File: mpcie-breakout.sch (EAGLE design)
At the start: 43 parts, among them K1 694108106102, U1 IP4234CZ6, U2 LD1085D2T33R, X1 MPCIE-JAE, X2 MINI-USB-SHIELD-UX60-MB-5ST

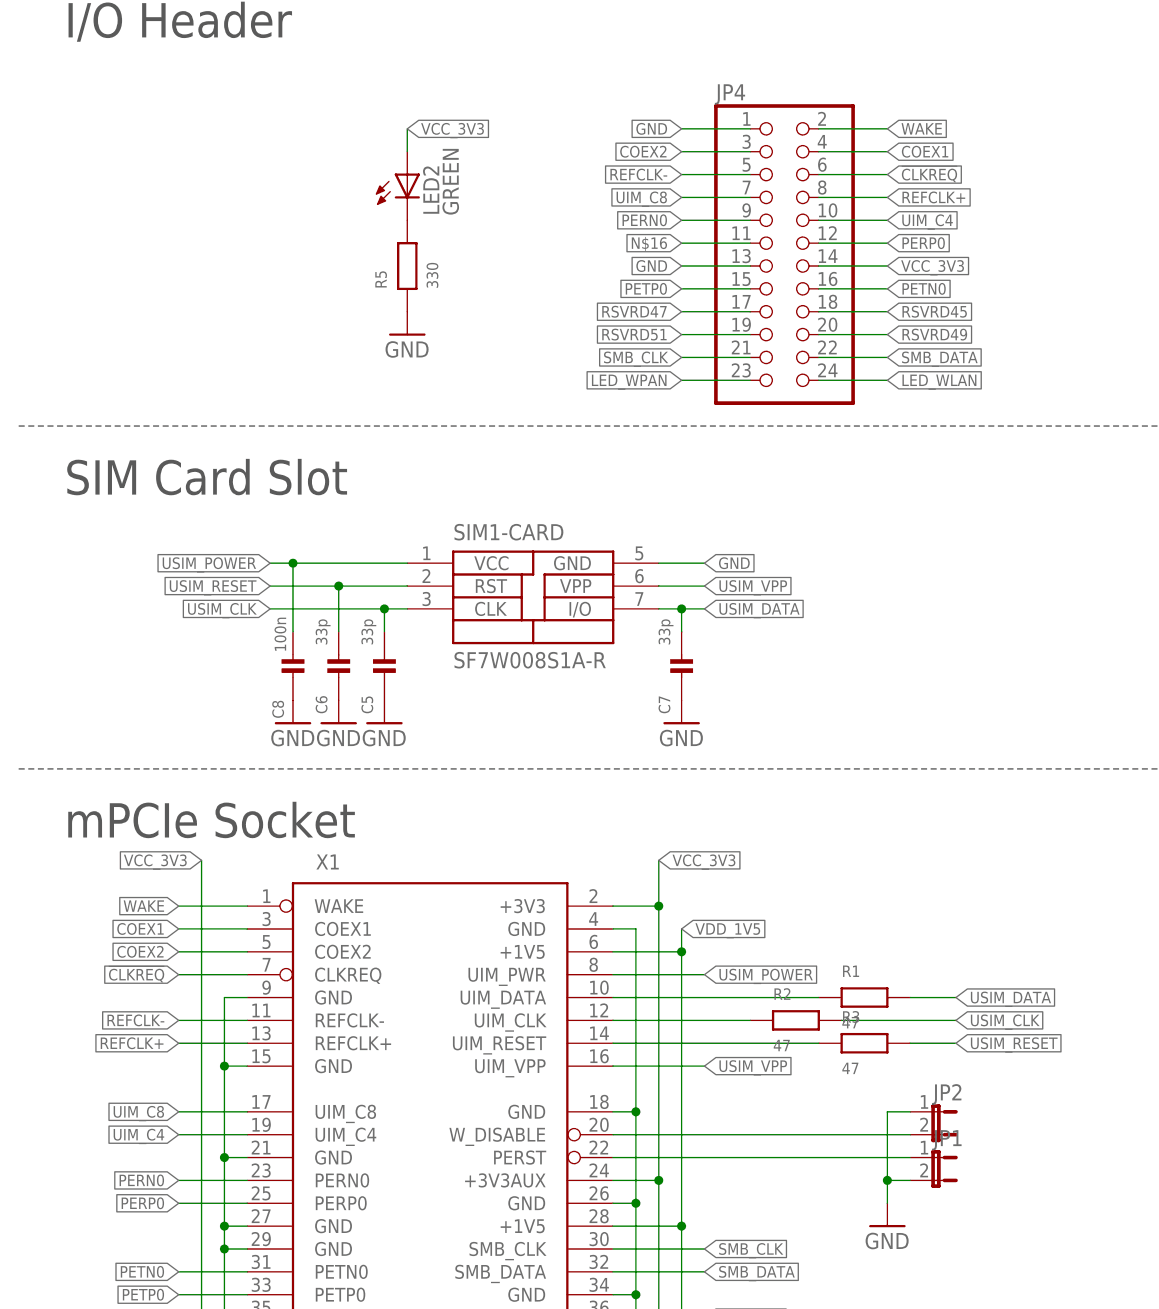
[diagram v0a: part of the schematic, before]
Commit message: added RXD, TXD, RTS, CTS
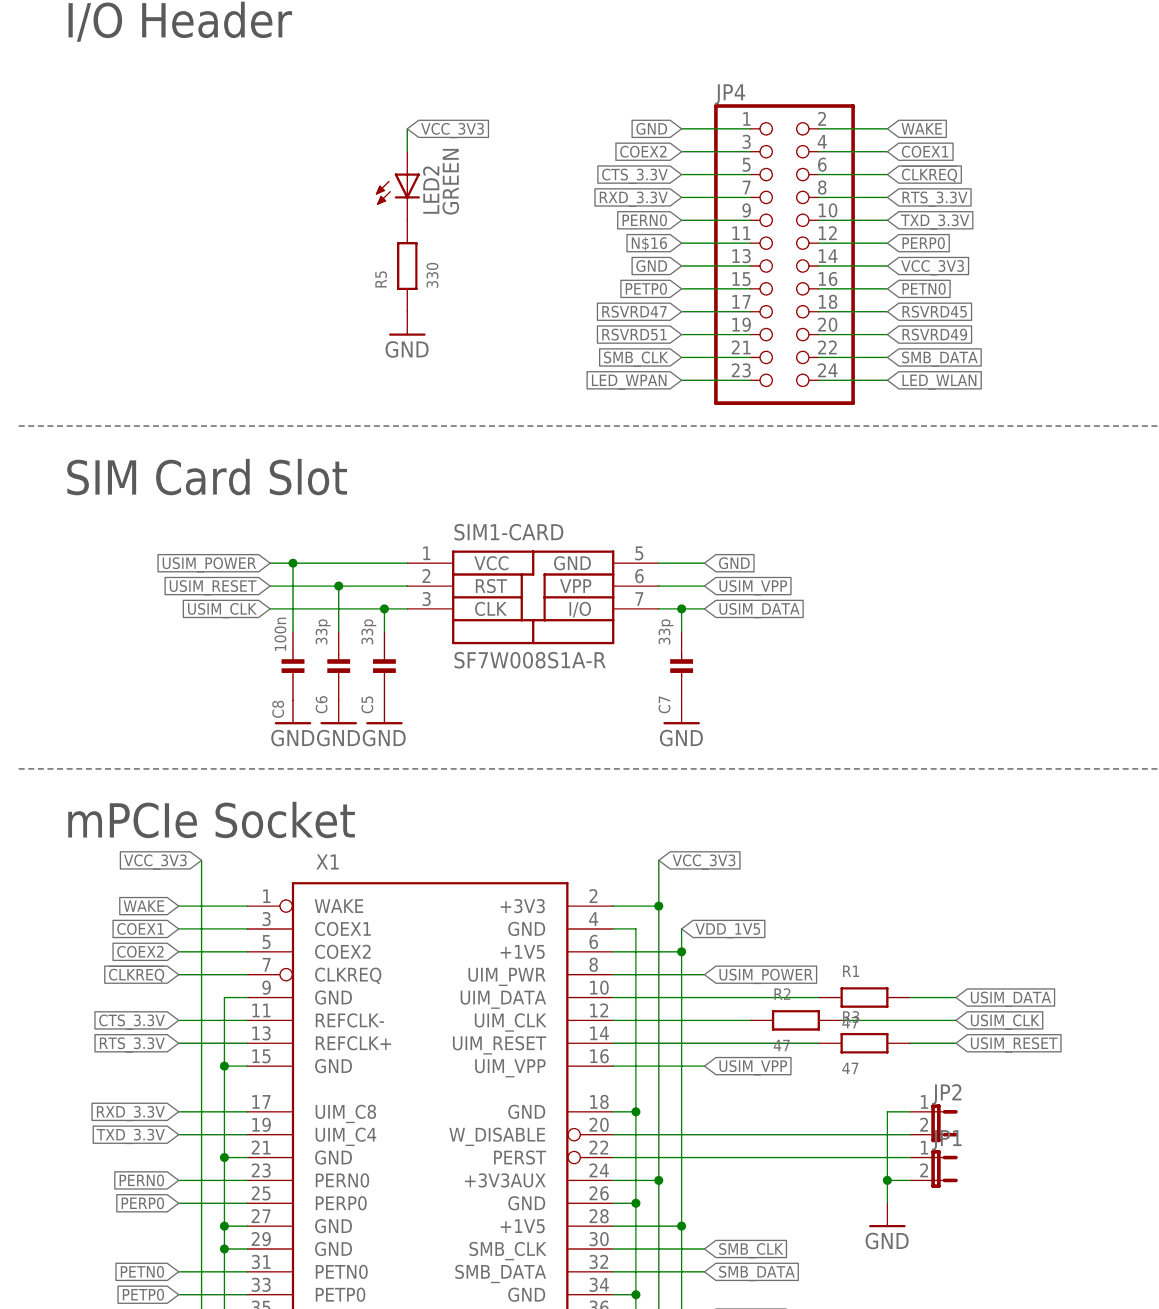
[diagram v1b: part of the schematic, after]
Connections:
- net REFCLK+ renamed RTS_3.3V
- net REFCLK- renamed CTS_3.3V
- net UIM_C4 renamed TXD_3.3V
- net UIM_C8 renamed RXD_3.3V
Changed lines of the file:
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@@
 </segment>
 </net>
-<net name="UIM_C8" class="0">
+<net name="RXD_3.3V" class="0">
 <segment>
 <pinref part="X1" gate="G$1" pin="UIM_C8"/>
@@
 </segment>
 </net>
-<net name="UIM_C4" class="0">
+<net name="TXD_3.3V" class="0">
 <segment>
 <pinref part="X1" gate="G$1" pin="UIM_C4"/>
@@
 </segment>
 </net>
-<net name="REFCLK-" class="0">
+<net name="CTS_3.3V" class="0">
 <segment>
 <pinref part="X1" gate="G$1" pin="REFCLK-"/>
@@
 </segment>
 </net>
-<net name="REFCLK+" class="0">
+<net name="RTS_3.3V" class="0">
 <segment>
 <pinref part="X1" gate="G$1" pin="REFCLK+"/>
